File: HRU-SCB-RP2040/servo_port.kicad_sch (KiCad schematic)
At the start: 36 parts, among them J1 Conn_01x03_Pin, J10 Conn_01x03_Pin, J11 Conn_01x03_Pin, J12 Conn_01x03_Pin, J13 Conn_01x03_Pin, J14 Conn_01x03_Pin, J15 Conn_01x03_Pin, J16 Conn_01x03_Pin, J17 Conn_01x03_Pin, J18 Conn_01x03_Pin, J19 Conn_01x03_Pin, J2 Conn_01x03_Pin, J20 Conn_01x03_Pin, J21 Conn_01x03_Pin, J22 Conn_01x03_Pin, J23 Conn_01x03_Pin, J24 Conn_01x03_Pin, J3 Conn_01x03_Pin, J4 Conn_01x03_Pin, J5 Conn_01x03_Pin, J6 Conn_01x03_Pin, J7 Conn_01x03_Pin, J8 Conn_01x03_Pin, J9 Conn_01x03_Pin, Q1 BS170, Q2 BS170, U2 MAX485E, U3 MAX485E

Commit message: Update: apply super DCDC
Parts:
- removed J10, J11, J12, J13, J14, J15, J16, J17, J18, J19, J2, J20, J21, J22, J23, J24, J3, J4, J5, J6, J7, J8, J9: Conn_01x03_Pin, mymod:PinHeader_1x03_P2.54mm_Vertical_SmallCourtyard, symbol Connector:Conn_01x03_Pin
- added S10, S11, S12, S13, S14, S15, S16, S17, S18, S19, S2, S20, S21, S22, S23, S24, S3, S4, S5, S6, S7, S8, S9: Conn_01x03_Pin, mymod:PinHeader_1x03_P2.54mm_Vertical_SmallCourtyard, symbol Connector:Conn_01x03_Pin
- Q1, Q2: footprint Package_TO_SOT_THT:TO-92_Inline_W4.0mm_Horizontal_FlatSideDown -> Package_TO_SOT_THT:TO-92_Inline
- renumbered R8 to R10, R1 to R3, R2 to R4, R3 to R5, R4 to R6, R5 to R7, R6 to R8, R7 to R9, J1 to S1, U2 to U1, U3 to U2
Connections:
- net GNDPWR: now also S10.3 (Pin_3), S11.3 (Pin_3), S12.3 (Pin_3), S13.3 (Pin_3), S14.3 (Pin_3), S15.3 (Pin_3), S16.3 (Pin_3), S17.3 (Pin_3), S18.3 (Pin_3), S19.3 (Pin_3), S2.3 (Pin_3), S20.3 (Pin_3), S21.3 (Pin_3), S22.3 (Pin_3), S23.3 (Pin_3), S24.3 (Pin_3), S3.3 (Pin_3), S4.3 (Pin_3), S5.3 (Pin_3), S6.3 (Pin_3), S7.3 (Pin_3), S8.3 (Pin_3), S9.3 (Pin_3)
- net SERVO.SERIAL0: now also S10.1 (Pin_1), S11.1 (Pin_1), S12.1 (Pin_1), S2.1 (Pin_1), S3.1 (Pin_1), S4.1 (Pin_1), S5.1 (Pin_1), S6.1 (Pin_1), S7.1 (Pin_1), S8.1 (Pin_1), S9.1 (Pin_1)
- net SERVO.SERIAL1: now also S13.1 (Pin_1), S14.1 (Pin_1), S15.1 (Pin_1), S16.1 (Pin_1), S17.1 (Pin_1), S18.1 (Pin_1), S19.1 (Pin_1), S20.1 (Pin_1), S21.1 (Pin_1), S22.1 (Pin_1), S23.1 (Pin_1), S24.1 (Pin_1)
- net VCC: now also S10.2 (Pin_2), S11.2 (Pin_2), S12.2 (Pin_2), S13.2 (Pin_2), S14.2 (Pin_2), S15.2 (Pin_2), S16.2 (Pin_2), S17.2 (Pin_2), S18.2 (Pin_2), S19.2 (Pin_2), S2.2 (Pin_2), S20.2 (Pin_2), S21.2 (Pin_2), S22.2 (Pin_2), S23.2 (Pin_2), S24.2 (Pin_2), S3.2 (Pin_2), S4.2 (Pin_2), S5.2 (Pin_2), S6.2 (Pin_2), S7.2 (Pin_2), S8.2 (Pin_2), S9.2 (Pin_2)

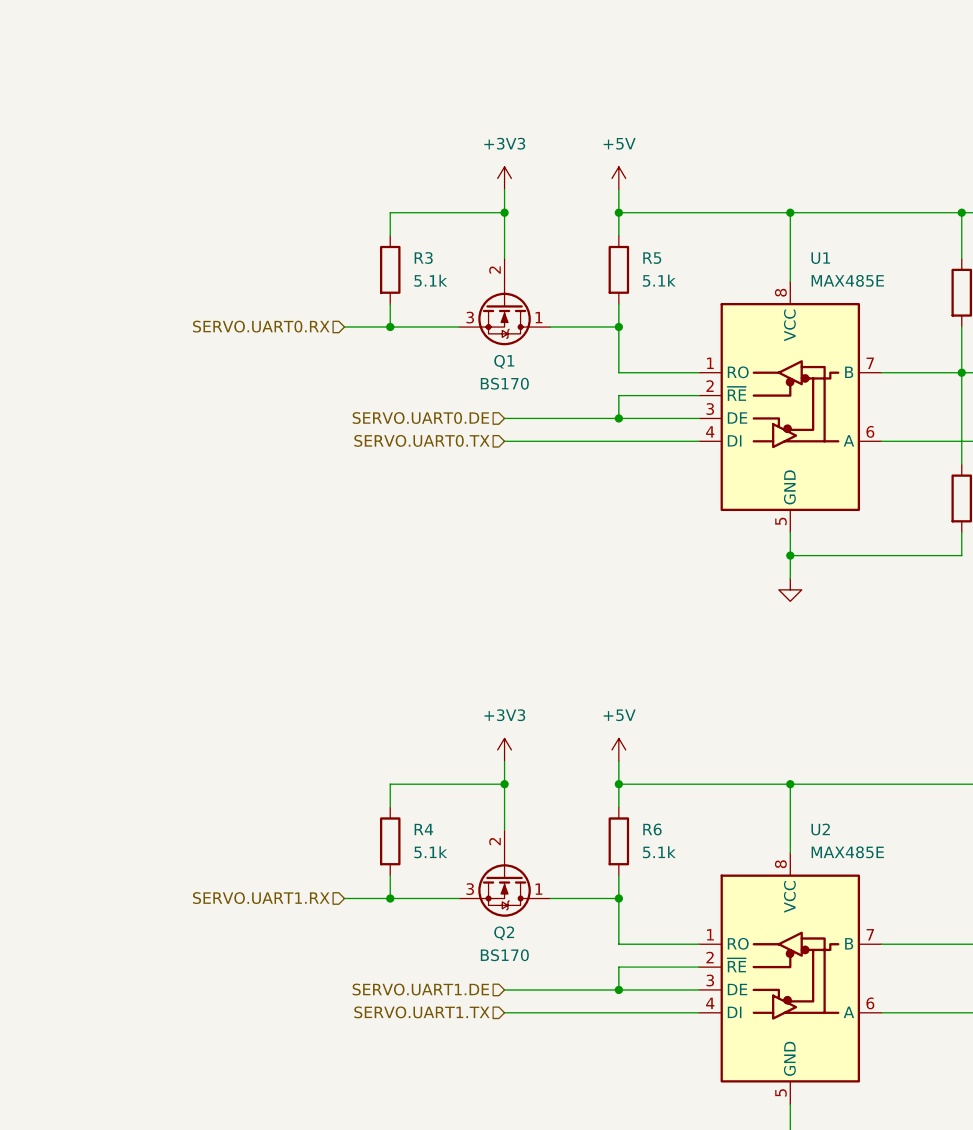
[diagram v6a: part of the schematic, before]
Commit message: fix(HRU-SCB-RP2040): add diodes for level shift
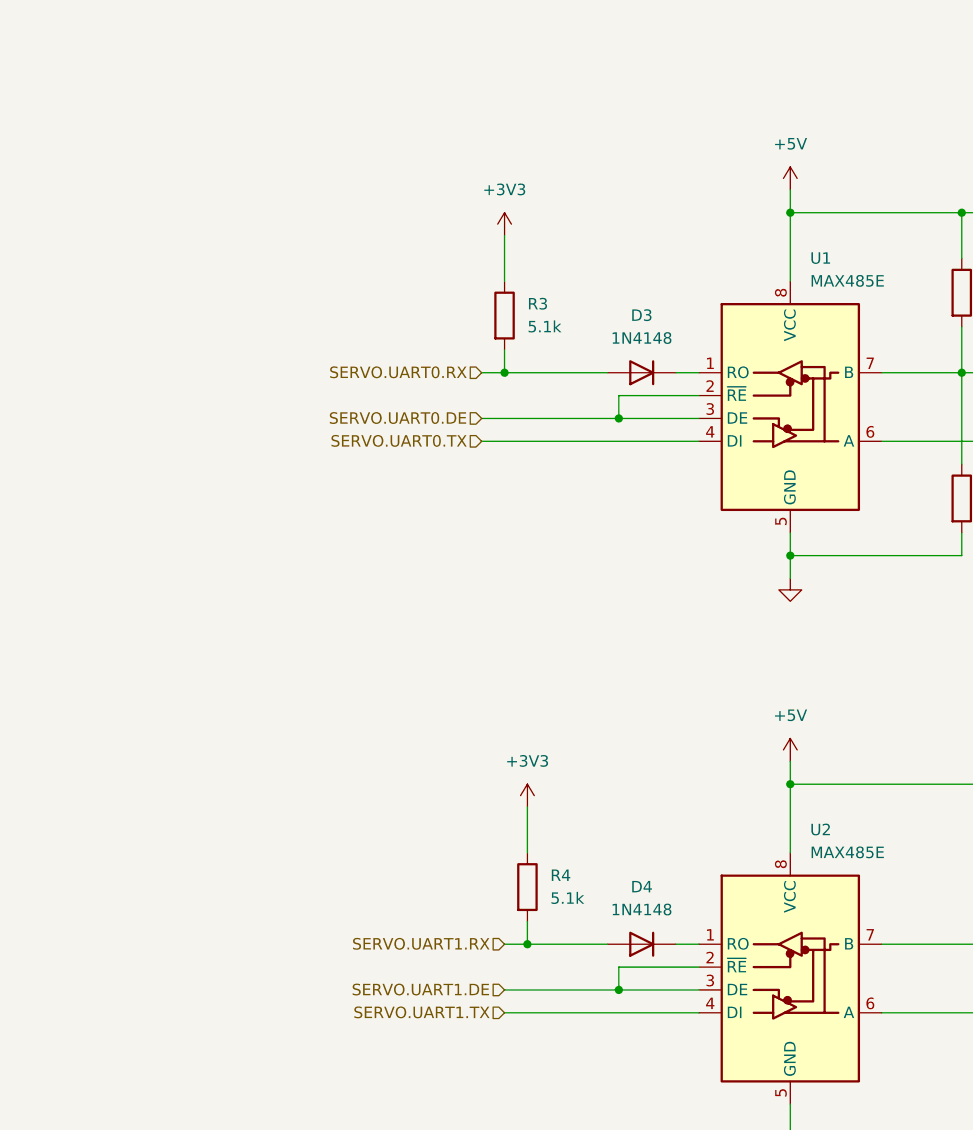
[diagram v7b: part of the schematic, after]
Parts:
- removed Q1, Q2: BS170, Package_TO_SOT_THT:TO-92_Inline, symbol Transistor_FET:BS170
- removed R5, R6: 5.1k, Resistor_THT:R_Axial_DIN0207_L6.3mm_D2.5mm_P7.62mm_Horizontal, symbol Device:R
- added D3, D4: 1N4148, Diode_THT:D_T-1_P5.08mm_Horizontal, symbol Diode:1N4148
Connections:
- net SERVO.UART0.RX: now also D3.2 (A)
- net SERVO.UART1.RX: now also D4.2 (A)
- net at U1.1 (RO): now also D3.1 (K)
- net at U2.1 (RO): now also D4.1 (K)
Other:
- moved on the sheet: R3
